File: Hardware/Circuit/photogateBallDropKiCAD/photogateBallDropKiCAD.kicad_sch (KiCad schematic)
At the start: 52 parts, among them Q1 2N3906, Q2 2N3904, Q3 2N3904, Q4 BPW40, Q5 2N3904, Q6 2N3904, Q7 2N3904, Q8 2N3904, SW2 SW_SPDT, U2 LM358

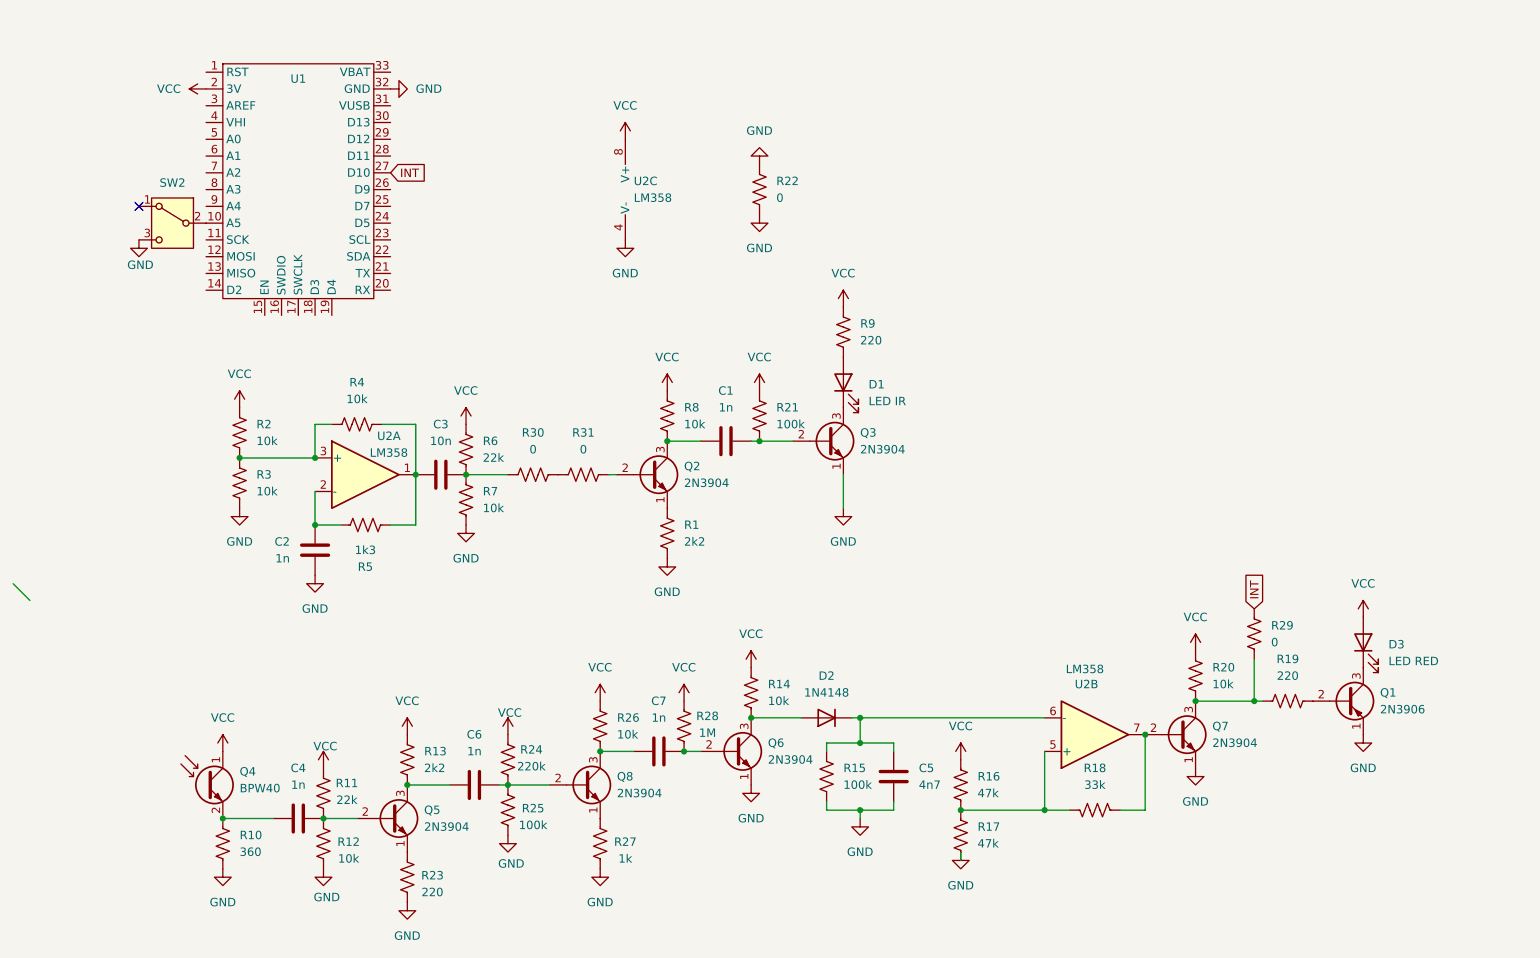
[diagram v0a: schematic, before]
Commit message: Add photogate PCB
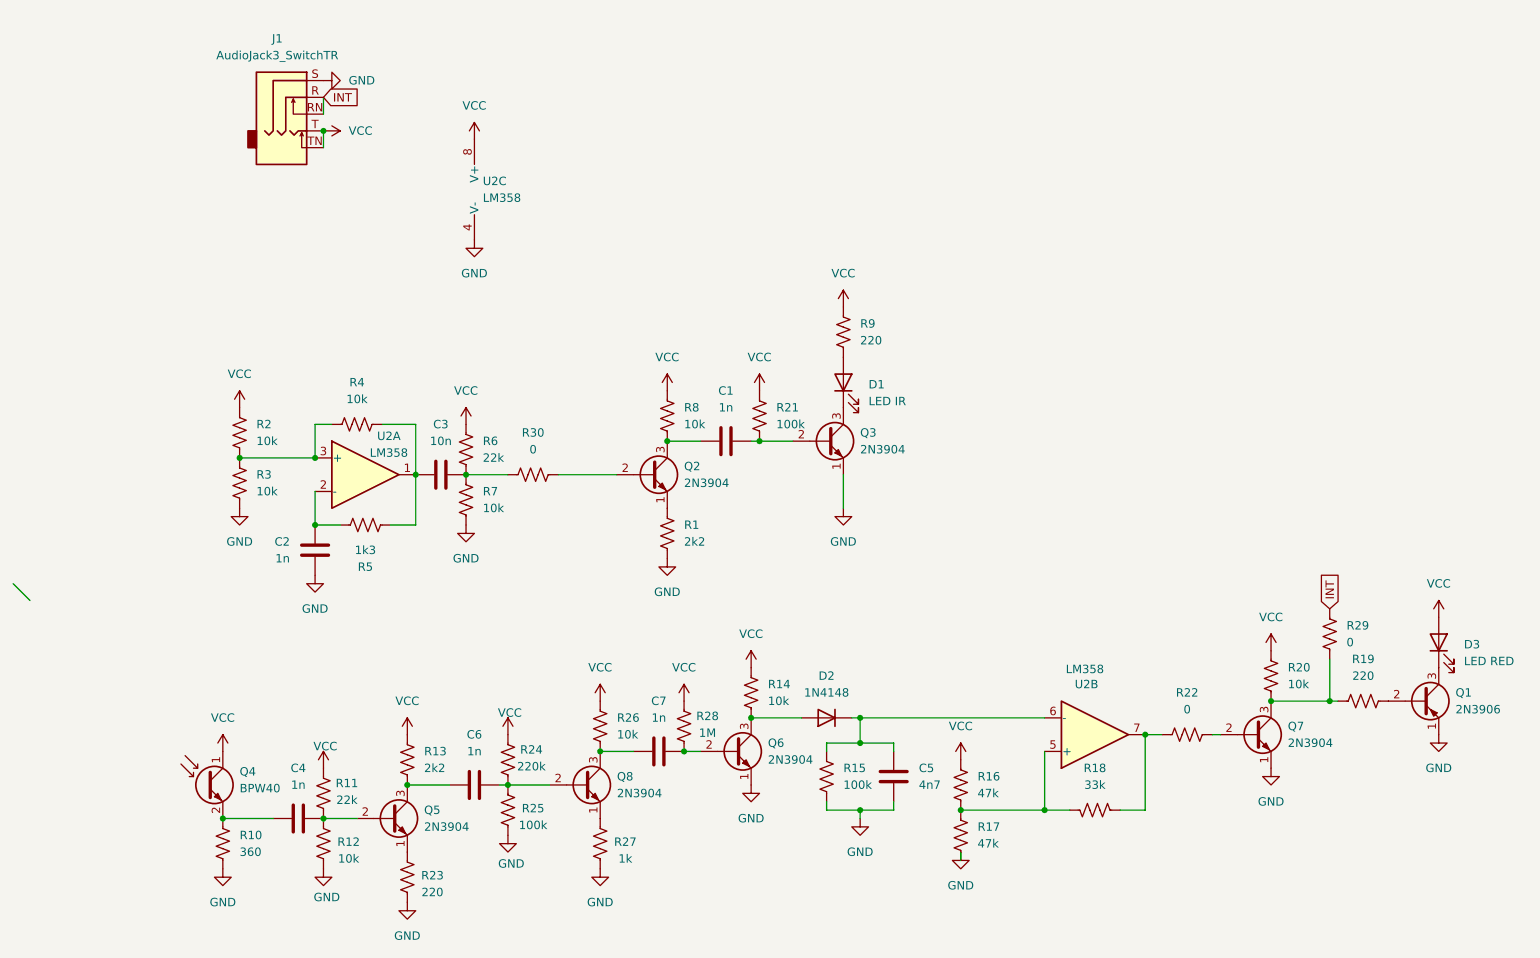
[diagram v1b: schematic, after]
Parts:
- removed R31: 0, Resistor_THT:R_Axial_DIN0207_L6.3mm_D2.5mm_P10.16mm_Horizontal, symbol Device:R_US
- removed SW2: SW_SPDT, User:SlideSwitch_SPDT, symbol Switch:SW_SPDT
- removed U1: ~, User:AdafruitItsyBitsyM0, symbol User:AdafruitItsyBitsyM0
- added J1: AudioJack3_SwitchTR, Connector_Audio:Jack_3.5mm_CUI_SJ1-3525N_Horizontal, symbol Connector_Audio:AudioJack3_SwitchTR
- R1: footprint Resistor_THT:R_Axial_DIN0207_L6.3mm_D2.5mm_P2.54mm_Vertical -> Resistor_THT:R_Axial_DIN0207_L6.3mm_D2.5mm_P7.62mm_Horizontal
- R21: footprint Resistor_THT:R_Axial_DIN0207_L6.3mm_D2.5mm_P7.62mm_Horizontal -> Resistor_THT:R_Axial_DIN0207_L6.3mm_D2.5mm_P5.08mm_Vertical
- R8: footprint Resistor_THT:R_Axial_DIN0207_L6.3mm_D2.5mm_P10.16mm_Horizontal -> Resistor_THT:R_Axial_DIN0207_L6.3mm_D2.5mm_P7.62mm_Horizontal
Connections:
- net GND: now also J1.S; no longer R22.1, R22.2
- net INT: now also J1.R, J1.RN
- net VCC: now also J1.T, J1.TN
- net at Q2.2 (B): now also R30.2
- net at R18.2, U2.7: now also R22.1; no longer Q7.2 (B)
- new net: Q7.2 (B), R22.2
- no-connect marks 1 -> 0
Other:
- moved on the sheet: D3, Q1, Q7, R19, R20, R29, U2C

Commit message: edit PCB
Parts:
- J1: footprint Connector_Audio:Jack_3.5mm_CUI_SJ1-3525N_Horizontal -> Connector_Audio:Jack_3.5mm_CUI_SJ1-3523N_Horizontal
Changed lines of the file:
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@@
 			)
 		)
-		(property "Footprint" "Connector_Audio:Jack_3.5mm_CUI_SJ1-3525N_Horizontal"
+		(property "Footprint" "Connector_Audio:Jack_3.5mm_CUI_SJ1-3523N_Horizontal"
 			(at 39.37 36.83 0)
 			(effects

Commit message: edit photogate pcb
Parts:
- removed C7: 1n, Capacitor_THT:C_Rect_L7.2mm_W2.5mm_P5.00mm_FKS2_FKP2_MKS2_MKP2, symbol Device:C
- removed J1: AudioJack3_SwitchTR, Connector_Audio:Jack_3.5mm_CUI_SJ1-3523N_Horizontal, symbol Connector_Audio:AudioJack3_SwitchTR
- removed Q6: 2N3904, Package_TO_SOT_THT:TO-92_Inline_Wide, symbol Transistor_BJT:2N3904
- removed R12, R14: 10k, Resistor_THT:R_Axial_DIN0207_L6.3mm_D2.5mm_P2.54mm_Vertical, symbol Device:R_US
- removed R21: 100k, Resistor_THT:R_Axial_DIN0207_L6.3mm_D2.5mm_P5.08mm_Vertical, symbol Device:R_US
- removed R22, R29, R30: 0, Resistor_THT:R_Axial_DIN0207_L6.3mm_D2.5mm_P10.16mm_Horizontal, symbol Device:R_US
- removed R23: 220, Resistor_THT:R_Axial_DIN0207_L6.3mm_D2.5mm_P2.54mm_Vertical, symbol Device:R_US
- removed R25: 100k, Resistor_THT:R_Axial_DIN0207_L6.3mm_D2.5mm_P2.54mm_Vertical, symbol Device:R_US
- removed R27: 1k, Resistor_THT:R_Axial_DIN0207_L6.3mm_D2.5mm_P2.54mm_Vertical, symbol Device:R_US
- removed R28: 1M, Resistor_THT:R_Axial_DIN0207_L6.3mm_D2.5mm_P2.54mm_Vertical, symbol Device:R_US
- added C10: 100u, Capacitor_THT:C_Radial_D8.0mm_H7.0mm_P3.50mm, symbol Device:C
- added C11: 1u, Capacitor_THT:C_Rect_L7.2mm_W2.5mm_P5.00mm_FKS2_FKP2_MKS2_MKP2, symbol Device:C
- added C12, C9: 10u, Capacitor_THT:C_Rect_L7.2mm_W2.5mm_P5.00mm_FKS2_FKP2_MKS2_MKP2, symbol Device:C
- added J1: AudioJack3, Connector_Audio:Jack_3.5mm_CUI_SJ1-3523N_Horizontal, symbol Connector_Audio:AudioJack3
- C1: value 1n -> 10n
- C3: value 10n -> 1n
- C5: value 4n7 -> 1n
- D2: footprint Diode_THT:D_DO-35_SOD27_P2.54mm_Vertical_AnodeUp -> Diode_THT:D_DO-35_SOD27_P7.62mm_Horizontal
- R1: value 2k2 -> 1k; footprint Resistor_THT:R_Axial_DIN0207_L6.3mm_D2.5mm_P7.62mm_Horizontal -> Resistor_THT:R_Axial_DIN0207_L6.3mm_D2.5mm_P10.16mm_Horizontal
- R10: value 360 -> 220; footprint Resistor_THT:R_Axial_DIN0207_L6.3mm_D2.5mm_P5.08mm_Vertical -> Resistor_THT:R_Axial_DIN0207_L6.3mm_D2.5mm_P7.62mm_Horizontal
- R11: value 22k -> 100k; footprint Resistor_THT:R_Axial_DIN0207_L6.3mm_D2.5mm_P2.54mm_Vertical -> Resistor_THT:R_Axial_DIN0207_L6.3mm_D2.5mm_P7.62mm_Horizontal
- R13: value 2k2 -> 10k; footprint Resistor_THT:R_Axial_DIN0207_L6.3mm_D2.5mm_P2.54mm_Vertical -> Resistor_THT:R_Axial_DIN0207_L6.3mm_D2.5mm_P7.62mm_Horizontal
- R15, R17, R4: footprint Resistor_THT:R_Axial_DIN0207_L6.3mm_D2.5mm_P5.08mm_Vertical -> Resistor_THT:R_Axial_DIN0207_L6.3mm_D2.5mm_P10.16mm_Horizontal
- R16: value 47k -> 100k; footprint Resistor_THT:R_Axial_DIN0207_L6.3mm_D2.5mm_P5.08mm_Vertical -> Resistor_THT:R_Axial_DIN0207_L6.3mm_D2.5mm_P10.16mm_Horizontal
- R18: value 33k -> 100k; footprint Resistor_THT:R_Axial_DIN0207_L6.3mm_D2.5mm_P5.08mm_Vertical -> Resistor_THT:R_Axial_DIN0207_L6.3mm_D2.5mm_P10.16mm_Horizontal
- R19: value 220 -> 1k; footprint Resistor_THT:R_Axial_DIN0207_L6.3mm_D2.5mm_P7.62mm_Horizontal -> Resistor_THT:R_Axial_DIN0207_L6.3mm_D2.5mm_P10.16mm_Horizontal
- R24: value 220k -> 1M; footprint Resistor_THT:R_Axial_DIN0207_L6.3mm_D2.5mm_P2.54mm_Vertical -> Resistor_THT:R_Axial_DIN0207_L6.3mm_D2.5mm_P7.62mm_Horizontal
- R26: footprint Resistor_THT:R_Axial_DIN0207_L6.3mm_D2.5mm_P2.54mm_Vertical -> Resistor_THT:R_Axial_DIN0207_L6.3mm_D2.5mm_P7.62mm_Horizontal
- R3: footprint Resistor_THT:R_Axial_DIN0207_L6.3mm_D2.5mm_P10.16mm_Horizontal -> Resistor_THT:R_Axial_DIN0207_L6.3mm_D2.5mm_P7.62mm_Horizontal
- R5: value 1k3 -> 1k; footprint Resistor_THT:R_Axial_DIN0207_L6.3mm_D2.5mm_P2.54mm_Vertical -> Resistor_THT:R_Axial_DIN0207_L6.3mm_D2.5mm_P7.62mm_Horizontal
- R6: value 22k -> 1M; footprint Resistor_THT:R_Axial_DIN0207_L6.3mm_D2.5mm_P10.16mm_Horizontal -> Resistor_THT:R_Axial_DIN0207_L6.3mm_D2.5mm_P7.62mm_Horizontal
- R7: value 10k -> 220
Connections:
- net GND: now also C1.1, Q2.1 (E), Q5.1 (E), Q8.1 (E), C10.1, C11.2, C12.1, C9.2, J1.S; no longer R1.2, R7.1
- net INT: now also Q7.3 (C), R20.2, J1.R
- net VCC: now also C1.2, R7.2, C10.2, C11.1, C12.2, C9.1, J1.T; no longer D3.2 (A)
- net at D2.2 (A): now also Q8.3 (C), R26.2
- net at C3.2, R6.2: now also Q2.2 (B); no longer R7.2
- net at R1.1: now also R18.2, R19.1, U2.7; no longer Q2.1 (E)
- net at Q2.3 (C), R8.2: now also Q3.2 (B); no longer C1.1
- net at Q7.2 (B): now also R1.2
- new net: D3.2 (A), R7.1
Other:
- moved on the sheet: C5, D1, D2, D3, Q1, Q2, Q3, Q7, R15, R16, R17, R18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

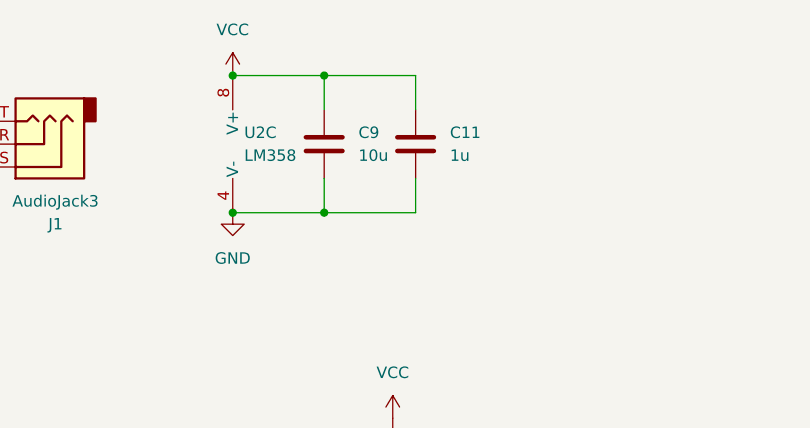
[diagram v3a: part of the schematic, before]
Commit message: Edit attachment point
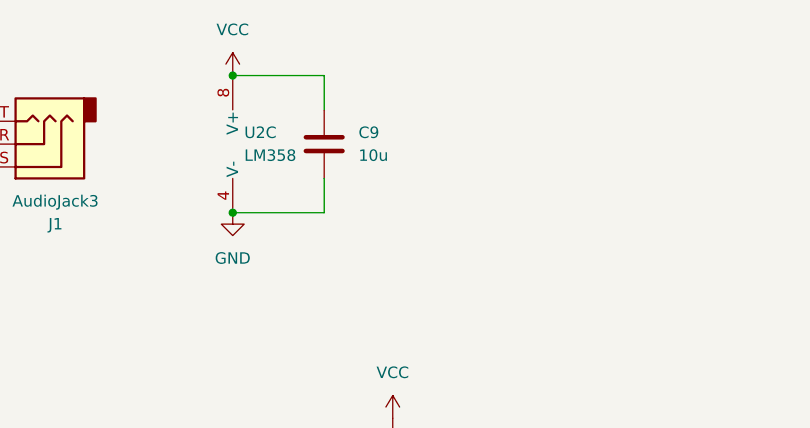
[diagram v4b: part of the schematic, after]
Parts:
- removed C11: 1u, Capacitor_THT:C_Rect_L7.2mm_W2.5mm_P5.00mm_FKS2_FKP2_MKS2_MKP2, symbol Device:C
- R1, R15, R16, R17, R18, R19, R4: footprint Resistor_THT:R_Axial_DIN0207_L6.3mm_D2.5mm_P10.16mm_Horizontal -> Resistor_THT:R_Axial_DIN0207_L6.3mm_D2.5mm_P7.62mm_Horizontal
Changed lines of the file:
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@@
 	)
 	(junction
-		(at 85.09 30.48)
-		(diameter 0)
-		(color 0 0 0 0)
-	)
-	(junction
 		(at 58.42 93.98)
 		(diameter 0)
@@
 	)
 	(junction
-		(at 85.09 45.72)
-		(diameter 0)
-		(color 0 0 0 0)
-	)
-	(junction
 		(at 184.15 133.35)
 		(diameter 0)
@@
 	(wire
 		(pts
-			(xy 95.25 41.91) (xy 95.25 45.72)
-		)
-		(stroke
-			(width 0)
-			(type default)
-		)
-	)
-	(wire
-		(pts
 			(xy 85.09 45.72) (xy 74.93 45.72)
 		)
@@
 	(wire
 		(pts
-			(xy 95.25 30.48) (xy 85.09 30.48)
-		)
-		(stroke
-			(width 0)
-			(type default)
-		)
-	)
-	(wire
-		(pts
 			(xy 58.42 101.6) (xy 58.42 93.98)
 		)
@@
 	(wire
 		(pts
-			(xy 95.25 45.72) (xy 85.09 45.72)
-		)
-		(stroke
-			(width 0)
-			(type default)
-		)
-	)
-	(wire
-		(pts
 			(xy 48.26 41.91) (xy 39.37 41.91)
 		)
@@
 	(wire
 		(pts
-			(xy 95.25 34.29) (xy 95.25 30.48)
-		)
-		(stroke
-			(width 0)
-			(type default)
-		)
-	)
-	(wire
-		(pts
 			(xy 48.26 41.91) (xy 48.26 40.64)
 		)
@@
 			)
 		)
-		(property "Footprint" "Resistor_THT:R_Axial_DIN0207_L6.3mm_D2.5mm_P10.16mm_Horizontal"
+		(property "Footprint" "Resistor_THT:R_Axial_DIN0207_L6.3mm_D2.5mm_P7.62mm_Horizontal"
 			(at 124.206 153.924 90)
 			(effects
@@
 			)
 		)
-		(property "Footprint" "Resistor_THT:R_Axial_DIN0207_L6.3mm_D2.5mm_P10.16mm_Horizontal"
+		(property "Footprint" "Resistor_THT:R_Axial_DIN0207_L6.3mm_D2.5mm_P7.62mm_Horizontal"
 			(at 172.974 137.414 90)
 			(effects
@@
 			)
 		)
-		(property "Footprint" "Resistor_THT:R_Axial_DIN0207_L6.3mm_D2.5mm_P10.16mm_Horizontal"
+		(property "Footprint" "Resistor_THT:R_Axial_DIN0207_L6.3mm_D2.5mm_P7.62mm_Horizontal"
 			(at 122.174 145.796 90)
 			(effects
@@
 			)
 		)
-		(property "Footprint" "Resistor_THT:R_Axial_DIN0207_L6.3mm_D2.5mm_P10.16mm_Horizontal"
+		(property "Footprint" "Resistor_THT:R_Axial_DIN0207_L6.3mm_D2.5mm_P7.62mm_Horizontal"
 			(at 198.374 148.844 90)
 			(effects
@@
 			)
 		)
-		(property "Footprint" "Resistor_THT:R_Axial_DIN0207_L6.3mm_D2.5mm_P10.16mm_Horizontal"
+		(property "Footprint" "Resistor_THT:R_Axial_DIN0207_L6.3mm_D2.5mm_P7.62mm_Horizontal"
 			(at 143.764 150.876 90)
 			(effects
@@
 	)
 	(symbol
-		(lib_id "Device:C")
-		(at 95.25 38.1 0)
-		(unit 1)
-		(exclude_from_sim no)
-		(in_bom yes)
-		(on_board yes)
-		(dnp no)
-		(fields_autoplaced yes)
-		(property "Reference" "C11"
-			(at 99.06 36.8299 0)
-			(effects
-				(font
-					(size 1.27 1.27)
-				)
-				(justify left)
-			)
-		)
-		(property "Value" "1u"
-			(at 99.06 39.3699 0)
-			(effects
-				(font
-					(size 1.27 1.27)
-				)
-				(justify left)
-			)
-		)
-		(property "Footprint" "Capacitor_THT:C_Rect_L7.2mm_W2.5mm_P5.00mm_FKS2_FKP2_MKS2_MKP2"
-			(at 96.2152 41.91 0)
-			(effects
-				(font
-					(size 1.27 1.27)
-				)
-				(hide yes)
-			)
-		)
-		(property "Datasheet" "~"
-			(at 95.25 38.1 0)
-			(effects
-				(font
-					(size 1.27 1.27)
-				)
-				(hide yes)
-			)
-		)
-		(property "Description" "Unpolarized capacitor"
-			(at 95.25 38.1 0)
-			(effects
-				(font
-					(size 1.27 1.27)
-				)
-				(hide yes)
-			)
-		)
-		(pin "2"
-		)
-		(pin "1"
-		)
-		(instances
-			(project "photogateBallDropKiCAD"
-				(path "/28efec4c-6083-4d69-b89b-ab16ee58a10e"
-					(reference "C11")
-					(unit 1)
-				)
-			)
-		)
-	)
-	(symbol
 		(lib_id "Device:R_US")
 		(at 44.45 142.24 0)
@@
 			)
 		)
-		(property "Footprint" "Resistor_THT:R_Axial_DIN0207_L6.3mm_D2.5mm_P10.16mm_Horizontal"
+		(property "Footprint" "Resistor_THT:R_Axial_DIN0207_L6.3mm_D2.5mm_P7.62mm_Horizontal"
 			(at 49.784 85.344 90)
 			(effects
@@
 			)
 		)
-		(property "Footprint" "Resistor_THT:R_Axial_DIN0207_L6.3mm_D2.5mm_P10.16mm_Horizontal"
+		(property "Footprint" "Resistor_THT:R_Axial_DIN0207_L6.3mm_D2.5mm_P7.62mm_Horizontal"
 			(at 103.886 145.034 90)
 			(effects
